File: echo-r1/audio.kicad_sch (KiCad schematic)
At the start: 28 parts, among them J4 HP_3.5mm, J5 LO_3.5mm, Q6 AO3401A, Q7 AO3401A, U9 TLV320AIC3104

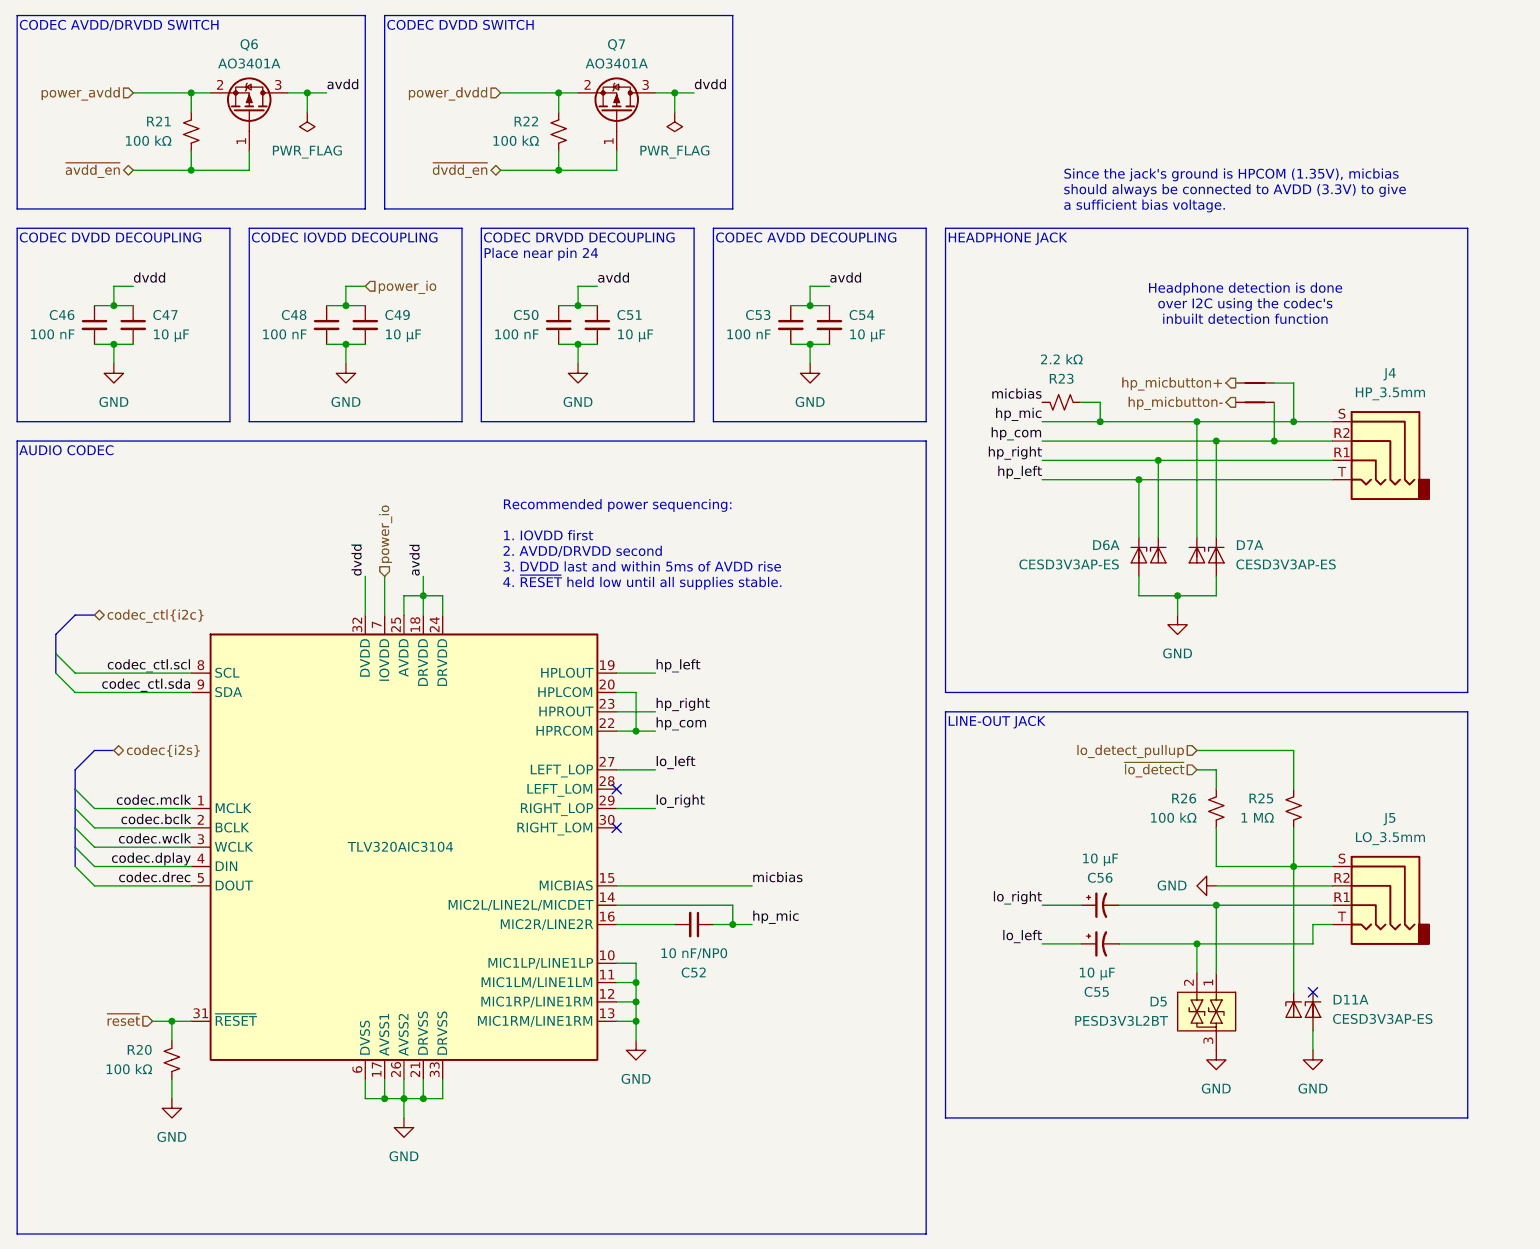
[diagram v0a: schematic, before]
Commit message: WIP redesign with STM32H7R3Z8J6
The H7R3 has a bunch of features that greatly simplify the design:
support for HyperRAM, which requires far fewer pins than SDRAM and
is more power efficient; this frees up the FMC to interface with the
display in 8-bit 8080 MCU mode; and there is a built-in USB HS PHY,
removing the need for an external PHY.

The huge reduction in signal count allows for a smaller pin count
package -- only 144 pins. HyperRAM only comes in BGA packages so it
makes sense to also use the UFBGA-144 package for the CPU, which
takes up less than 1/4 of the board area of an LQFP-176 package.
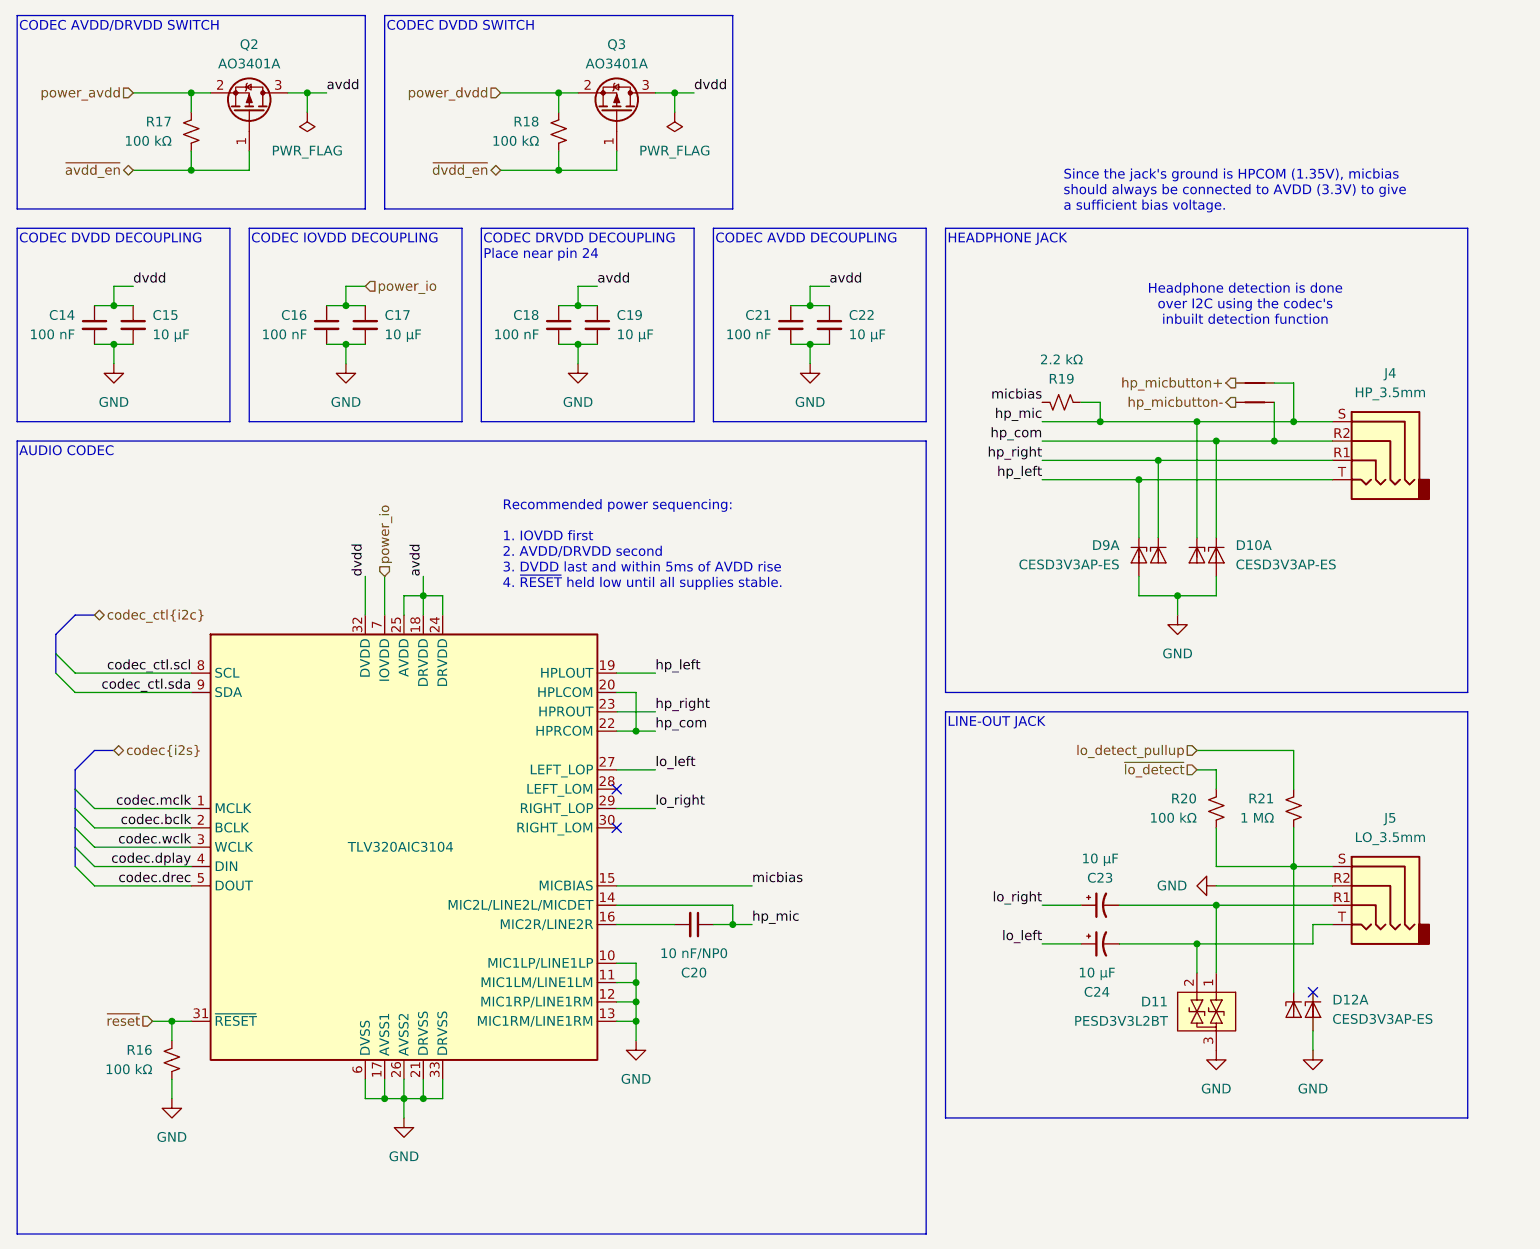
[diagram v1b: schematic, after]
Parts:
- renumbered C46 to C14, C47 to C15, C48 to C16, C49 to C17, C50 to C18, C51 to C19, C52 to C20, C53 to C21, C54 to C22, C56 to C23, C55 to C24, D7 to D10, D5 to D11, D11 to D12, D6 to D9, Q6 to Q2, Q7 to Q3, R20 to R16, R21 to R17, R22 to R18, R23 to R19, R26 to R20, R25 to R21, U9 to U6

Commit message: Continue with redesign, update and simplify schematic
- Consolidate small sheets (ports, etc) onto one page
- Add placeholders for STM32 external components
- Add power switch on SD card for resetting it
- Fix oversized input capacitors on voltage regulators
- Get rid of unique 1M resistor used in line-out detection
- Remove SOT23 TVS diodes (will be replaced by another package)
- Update LCD connector symbol for new 30pin screen
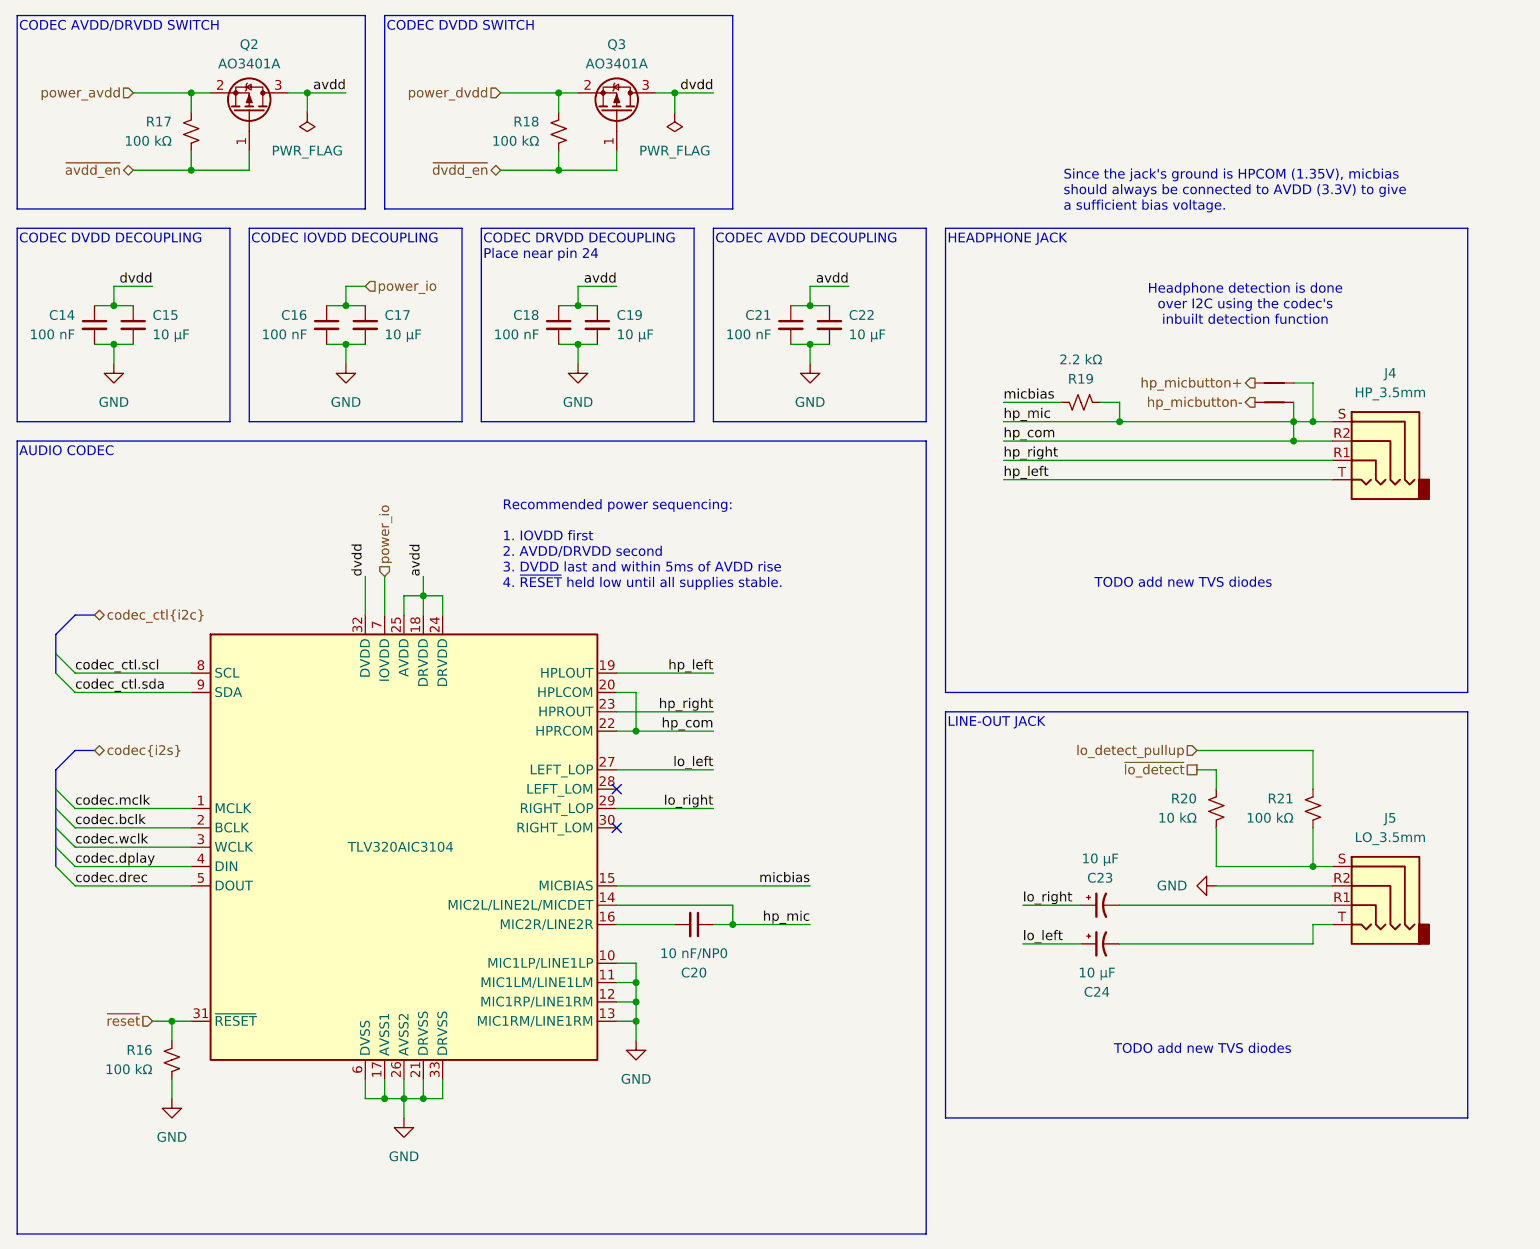
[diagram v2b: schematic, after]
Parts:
- removed D10, D12, D9: CESD3V3AP-ES, Package_TO_SOT_SMD:SOT-23, symbol echoplayer:CESD3V3AP-ES
- removed D11: PESD3V3L2BT, Package_TO_SOT_SMD:SOT-23, symbol echoplayer:PESD3V3L2BT
- R20: value 100 kΩ -> 10 kΩ
- R21: value 1 MΩ -> 100 kΩ
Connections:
- net hp_mic is gone; now on net hp_com: C20.1, J4.S, NT1.2, R19.2, U6.14 (MIC2L/LINE2L/MICDET)
- no-connect marks 3 -> 2
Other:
- note added: "TODO add new TVS diodes"
- moved on the sheet: R19, R21
